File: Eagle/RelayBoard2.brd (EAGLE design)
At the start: 100 x 80 mm, 4 parts, among them K1 4052, X2 MKDSN1,5/3-5,08, X3 MKDSN1,5/3-5,08

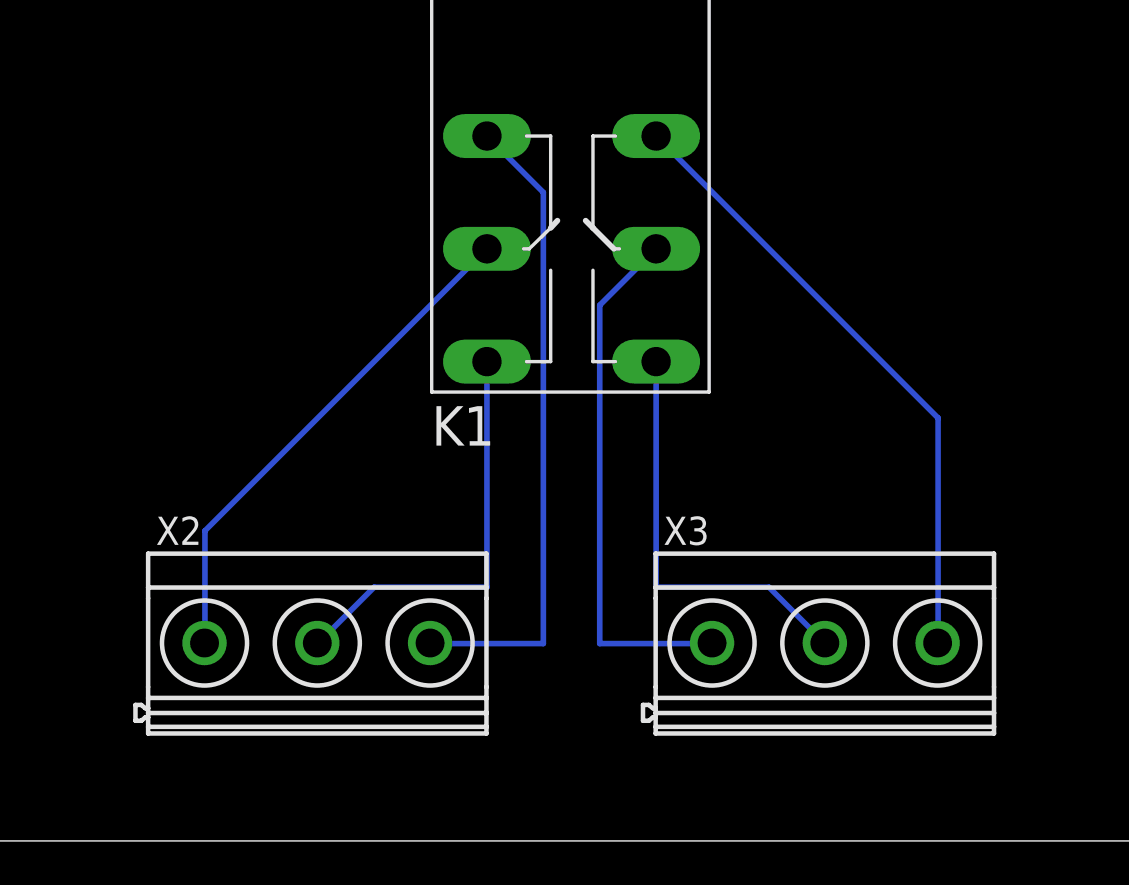
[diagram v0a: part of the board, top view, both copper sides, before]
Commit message: - correction to RelayBoard2 - added schematic for PowerSupply (no board so far)
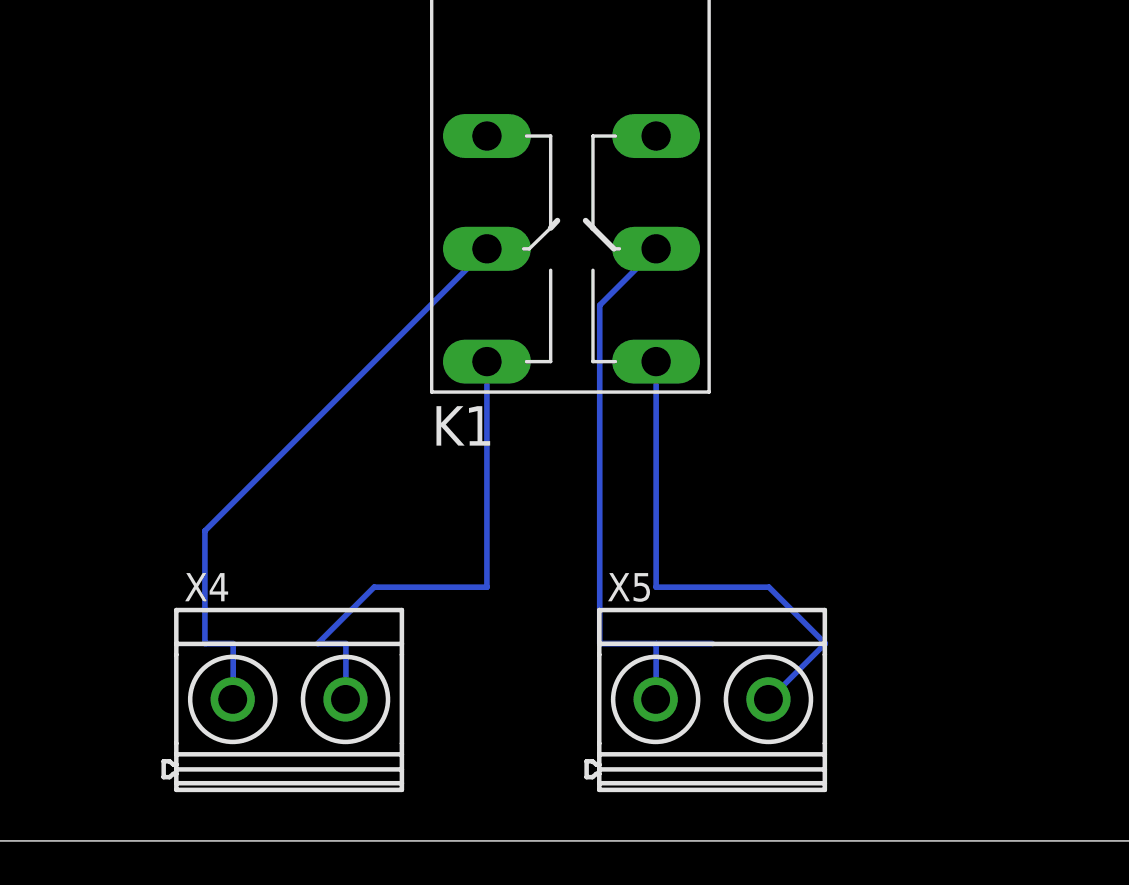
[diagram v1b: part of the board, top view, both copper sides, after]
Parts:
- removed X2, X3: MKDSN1,5/3-5,08, con-phoenix-508:MKDSN1,5/3-5,08
- added X4, X5: MKDSN1,5/2-5,08, con-phoenix-508:MKDSN1,5/2-5,08
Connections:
- removed net N$1: K1.O2, X3.3
- removed net N$5: K1.O1, X2.3
- net N$3: now also X5.1; no longer X3.1
- net N$4: now also X5.2; no longer X3.2
- net N$6: now also X4.2; no longer X2.2
- net N$7: now also X4.1; no longer X2.1
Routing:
- net N$5: track 29.0 -> 0.00 mm
- net N$1: track 28.2 -> 0.00 mm
- net N$7: track 23.1 -> 26.9 mm
- net N$6: track 18.9 -> 22.7 mm
- net N$4: track 18.9 -> 22.5 mm
- net N$3: track 23.9 -> 26.5 mm
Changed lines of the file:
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@@
 <attribute name="OC_FARNELL" value="unknown" x="24.13" y="3.81" size="1.778" layer="27" rot="R270" display="off"/>
 </element>
-<element name="X2" library="con-phoenix-508" package="MKDSN1,5/3-5,08" value="MKDSN1,5/3-5,08" x="22.86" y="8.89">
-<attribute name="OC_NEWARK" value="70R0299" x="46.99" y="-10.16" size="1.778" layer="27" display="off"/>
-<attribute name="MPN" value="SMKDSN1,5/3-5,08" x="46.99" y="-10.16" size="1.778" layer="27" display="off"/>
-<attribute name="MF" value="" x="46.99" y="-10.16" size="1.778" layer="27" display="off"/>
-<attribute name="OC_FARNELL" value="1792904" x="46.99" y="-10.16" size="1.778" layer="27" display="off"/>
+<element name="X4" library="con-phoenix-508" package="MKDSN1,5/2-5,08" value="MKDSN1,5/2-5,08" x="19.05" y="6.35">
+<attribute name="OC_NEWARK" value="30M2397" x="19.05" y="6.35" size="1.778" layer="27" display="off"/>
+<attribute name="MPN" value="MKDSN 1,5/2-5.08" x="19.05" y="6.35" size="1.778" layer="27" display="off"/>
+<attribute name="MF" value="" x="19.05" y="6.35" size="1.778" layer="27" display="off"/>
+<attribute name="OC_FARNELL" value="1792903" x="19.05" y="6.35" size="1.778" layer="27" display="off"/>
 </element>
-<element name="X3" library="con-phoenix-508" package="MKDSN1,5/3-5,08" value="MKDSN1,5/3-5,08" x="45.72" y="8.89">
-<attribute name="OC_NEWARK" value="70R0299" x="69.85" y="-21.59" size="1.778" layer="27" display="off"/>
-<attribute name="MPN" value="SMKDSN1,5/3-5,08" x="69.85" y="-21.59" size="1.778" layer="27" display="off"/>
-<attribute name="MF" value="" x="69.85" y="-21.59" size="1.778" layer="27" display="off"/>
-<attribute name="OC_FARNELL" value="1792904" x="69.85" y="-21.59" size="1.778" layer="27" display="off"/>
+<element name="X5" library="con-phoenix-508" package="MKDSN1,5/2-5,08" value="MKDSN1,5/2-5,08" x="38.1" y="6.35">
+<attribute name="OC_NEWARK" value="30M2397" x="38.1" y="6.35" size="1.778" layer="27" display="off"/>
+<attribute name="MPN" value="MKDSN 1,5/2-5.08" x="38.1" y="6.35" size="1.778" layer="27" display="off"/>
+<attribute name="MF" value="" x="38.1" y="6.35" size="1.778" layer="27" display="off"/>
+<attribute name="OC_FARNELL" value="1792903" x="38.1" y="6.35" size="1.778" layer="27" display="off"/>
 </element>
 </elements>
@@
 </signal>
 <signal name="N$3">
-<contactref element="X3" pad="1"/>
 <contactref element="K1" pad="P2"/>
 <wire x1="33.02" y1="24.13" x2="35.56" y2="26.67" width="0.254" layer="16"/>
 <wire x1="33.02" y1="8.89" x2="33.02" y2="24.13" width="0.254" layer="16"/>
-<wire x1="38.1" y1="8.89" x2="33.02" y2="8.89" width="0.254" layer="16"/>
-<wire x1="38.1" y1="8.89" x2="38.0789" y2="8.915" width="0.254" layer="16"/>
+<wire x1="38.1" y1="8.89" x2="35.56" y2="8.89" width="0.254" layer="16"/>
+<contactref element="X5" pad="1"/>
+<wire x1="35.56" y1="8.89" x2="33.02" y2="8.89" width="0.254" layer="16"/>
+<wire x1="35.56" y1="8.89" x2="35.56" y2="6.35" width="0.254" layer="16"/>
+<wire x1="35.56" y1="6.35" x2="35.5389" y2="6.375" width="0.254" layer="16"/>
 </signal>
 <signal name="N$4">
 <contactref element="K1" pad="S2"/>
-<contactref element="X3" pad="2"/>
 <wire x1="35.56" y1="11.43" x2="35.56" y2="21.59" width="0.254" layer="16"/>
 <wire x1="40.64" y1="11.43" x2="35.56" y2="11.43" width="0.254" layer="16"/>
 <wire x1="43.18" y1="8.89" x2="40.64" y2="11.43" width="0.254" layer="16"/>
-<wire x1="43.18" y1="8.89" x2="43.1589" y2="8.915" width="0.254" layer="16"/>
-</signal>
-<signal name="N$1">
-<contactref element="X3" pad="3"/>
-<contactref element="K1" pad="O2"/>
-<wire x1="48.26" y1="19.05" x2="35.56" y2="31.75" width="0.254" layer="16"/>
-<wire x1="48.26" y1="8.89" x2="48.26" y2="19.05" width="0.254" layer="16"/>
-<wire x1="48.26" y1="8.89" x2="48.2389" y2="8.915" width="0.254" layer="16"/>
-</signal>
-<signal name="N$5">
-<contactref element="X2" pad="3"/>
-<contactref element="K1" pad="O1"/>
-<wire x1="30.48" y1="29.21" x2="27.94" y2="31.75" width="0.254" layer="16"/>
-<wire x1="30.48" y1="8.89" x2="30.48" y2="29.21" width="0.254" layer="16"/>
-<wire x1="25.4" y1="8.89" x2="30.48" y2="8.89" width="0.254" layer="16"/>
-<wire x1="25.4" y1="8.89" x2="25.3789" y2="8.915" width="0.254" layer="16"/>
+<contactref element="X5" pad="2"/>
+<wire x1="43.18" y1="8.89" x2="40.64" y2="6.35" width="0.254" layer="16"/>
+<wire x1="40.64" y1="6.35" x2="40.6189" y2="6.375" width="0.254" layer="16"/>
 </signal>
 <signal name="N$6">
-<contactref element="X2" pad="2"/>
 <contactref element="K1" pad="S1"/>
 <wire x1="27.94" y1="11.43" x2="27.94" y2="21.59" width="0.254" layer="16"/>
 <wire x1="22.86" y1="11.43" x2="27.94" y2="11.43" width="0.254" layer="16"/>
 <wire x1="20.32" y1="8.89" x2="22.86" y2="11.43" width="0.254" layer="16"/>
-<wire x1="20.32" y1="8.89" x2="20.2989" y2="8.915" width="0.254" layer="16"/>
+<contactref element="X4" pad="2"/>
+<wire x1="21.59" y1="8.89" x2="21.59" y2="6.35" width="0.254" layer="16"/>
+<wire x1="20.32" y1="8.89" x2="21.59" y2="8.89" width="0.254" layer="16"/>
+<wire x1="21.59" y1="6.35" x2="21.5689" y2="6.375" width="0.254" layer="16"/>
 </signal>
 <signal name="N$7">
-<contactref element="X2" pad="1"/>
 <contactref element="K1" pad="P1"/>
 <wire x1="15.24" y1="13.97" x2="27.94" y2="26.67" width="0.254" layer="16"/>
 <wire x1="15.24" y1="8.89" x2="15.24" y2="13.97" width="0.254" layer="16"/>
-<wire x1="15.24" y1="8.89" x2="15.2189" y2="8.915" width="0.254" layer="16"/>
+<contactref element="X4" pad="1"/>
+<wire x1="16.51" y1="8.89" x2="16.51" y2="6.35" width="0.254" layer="16"/>
+<wire x1="15.24" y1="8.89" x2="16.51" y2="8.89" width="0.254" layer="16"/>
+<wire x1="16.51" y1="6.35" x2="16.4889" y2="6.375" width="0.254" layer="16"/>
 </signal>
 </signals>
